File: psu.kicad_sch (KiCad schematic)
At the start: 30 parts, among them U1 TLS115, U3 LMR14020, U4 TJA1051T-3, U5 TJA1051T-3, U6 AMS1117-3.3

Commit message: update
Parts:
- added D19: SM15T33CA, Diode_SMD:D_SMC, symbol Device:D_TVS
- added D20: D_Schottky, Diode_SMD:D_SMA, symbol Device:D_Schottky
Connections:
- net 12v_PROT: now also D20.1 (K)
- net GND: now also D19.2 (A2)
- new net 12V_MR: D19.1 (A1), D20.2 (A)
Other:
- moved on the sheet: C2, C3, R1, U1

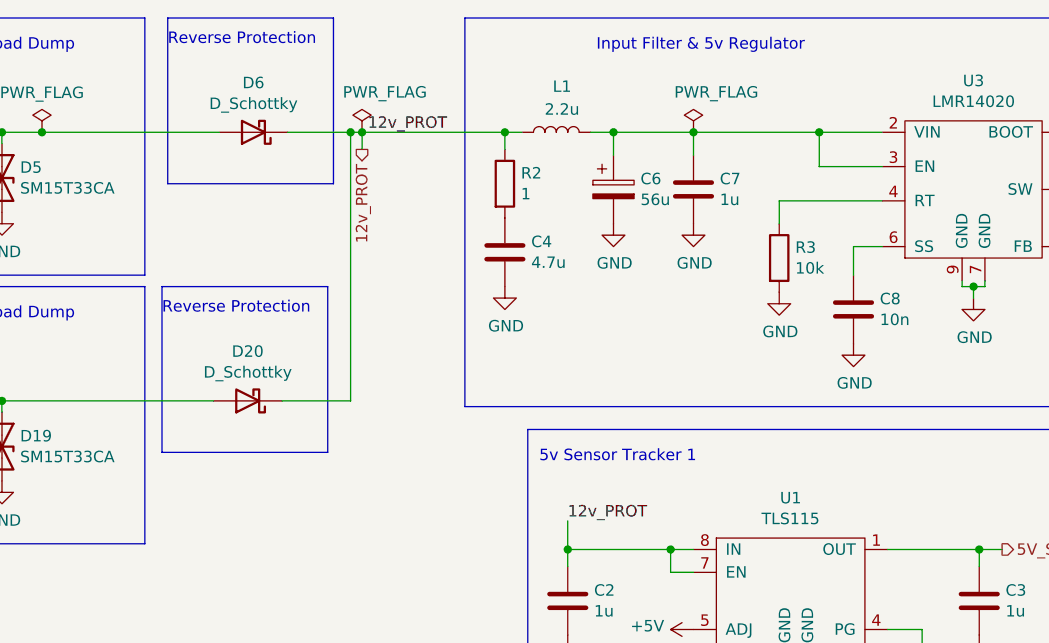
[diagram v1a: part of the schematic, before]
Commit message: Updates - Route digital inputs to connector - Add optional VR conditioner - Second Enable for H-Bridge
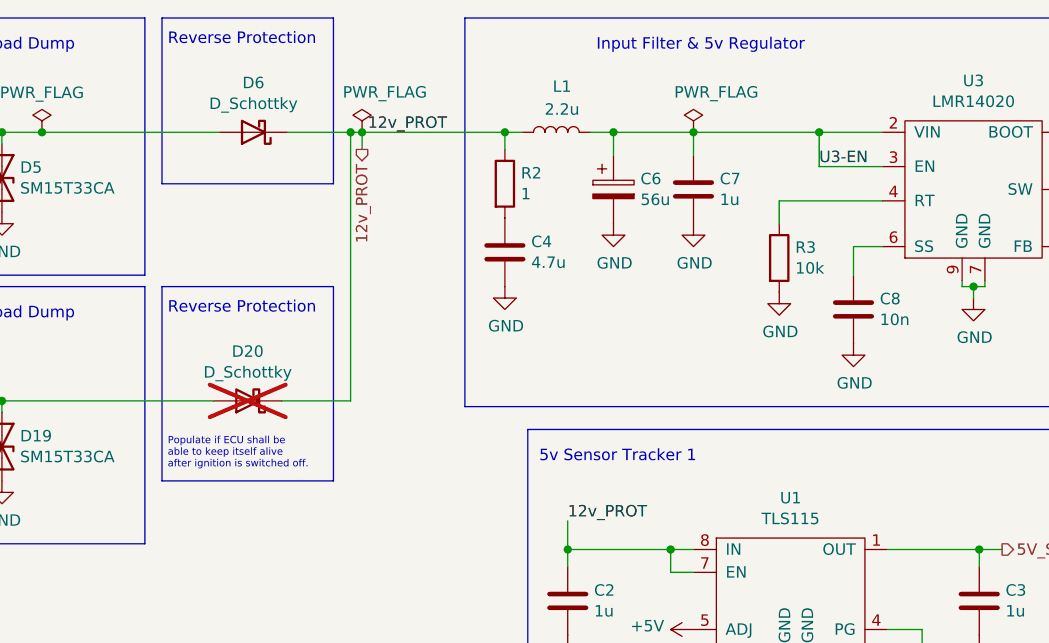
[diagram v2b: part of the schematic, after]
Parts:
- D20: now not fitted
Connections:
- net U3-EN: now reaches C6.1, C7.1, L1.2, U3.2 (VIN), U3.3 (EN)
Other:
- note added: "Populate if ECU shall be able to keep itself alive after ignition is switched off."
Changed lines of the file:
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@@
     (stroke (width 0) (type default))
   )
-  (polyline (pts (xy 50.165 16.51) (xy 68.58 16.51))
+  (polyline (pts (xy 49.53 16.51) (xy 68.58 16.51))
     (stroke (width 0) (type default))
   )
@@
     (stroke (width 0) (type default))
   )
-  (polyline (pts (xy 67.945 46.355) (xy 67.945 64.77))
+  (polyline (pts (xy 68.58 46.355) (xy 68.58 67.945))
     (stroke (width 0) (type default))
   )
@@
     (stroke (width 0) (type default))
   )
-  (polyline (pts (xy 49.53 46.355) (xy 67.945 46.355))
-    (stroke (width 0) (type default))
-  )
-  (polyline (pts (xy 68.58 34.925) (xy 50.165 34.925))
+  (polyline (pts (xy 49.53 46.355) (xy 68.58 46.355))
+    (stroke (width 0) (type default))
+  )
+  (polyline (pts (xy 68.58 34.925) (xy 49.53 34.925))
     (stroke (width 0) (type default))
   )
@@
     (stroke (width 0) (type default))
   )
-  (polyline (pts (xy 50.165 34.925) (xy 50.165 16.51))
+  (polyline (pts (xy 49.53 34.925) (xy 49.53 16.51))
     (stroke (width 0) (type default))
   )
@@
     (stroke (width 0) (type default))
   )
-  (polyline (pts (xy 67.945 64.77) (xy 49.53 64.77))
+  (polyline (pts (xy 68.58 67.945) (xy 49.53 67.945))
     (stroke (width 0) (type default))
   )
@@
     (stroke (width 0) (type default))
   )
-  (polyline (pts (xy 49.53 64.77) (xy 49.53 46.355))
+  (polyline (pts (xy 49.53 67.945) (xy 49.53 46.355))
     (stroke (width 0) (type default))
   )
@@
     (stroke (width 0) (type default))
   )
-  (text "Reverse Protection" (at 49.53 49.53 0)
+  (text "Populate if ECU shall be \nable to keep itself alive\nafter ignition is switched off."
+    (at 50.165 66.675 0)
+    (effects (font (size 0.8 0.8)) (justify left bottom))
+  )
+  (text "Reverse Protection" (at 50.165 49.53 0)
     (effects (font (size 1.27 1.27)) (justify left bottom))
   )
@@
   )
   (label "12v_PROT" (at 94.615 72.39 0) (fields_autoplaced)
+    (effects (font (size 1.27 1.27)) (justify left bottom))
+  )
+  (label "U3-EN" (at 122.555 33.02 0) (fields_autoplaced)
     (effects (font (size 1.27 1.27)) (justify left bottom))
   )
@@
   )
   (symbol (lib_id "Device:D_Schottky") (at 59.055 59.055 180) (unit 1)
-    (in_bom yes) (on_board yes) (dnp no)
+    (in_bom yes) (on_board yes) (dnp yes)
     (property "Reference" "D20" (at 59.055 53.5686 0)
       (effects (font (size 1.27 1.27)))

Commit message: USB jack, parts and LCSC numbers, headphone jack
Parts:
- C6: LCSC N/A -> C106564
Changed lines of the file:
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@@
       (effects (font (size 1.27 1.27)) hide)
     )
-    (property "LCSC" "N/A" (at 99.695 35.56 0)
+    (property "LCSC" "C106564" (at 99.695 35.56 0)
       (effects (font (size 1.27 1.27)) hide)
     )

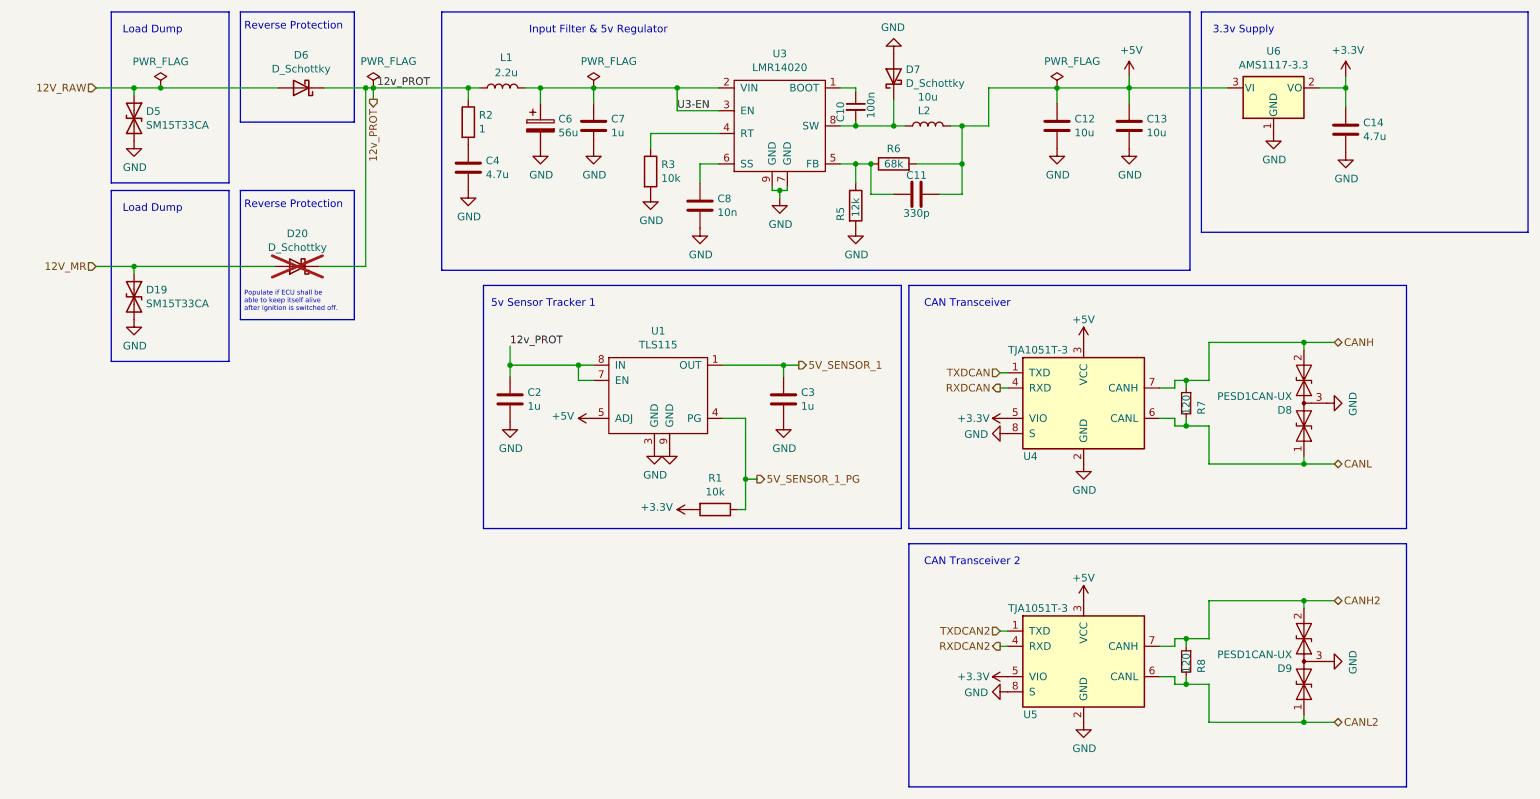
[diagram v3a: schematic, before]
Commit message: Add power LEDs, silkscreen beautifying, remove U11 use U10B
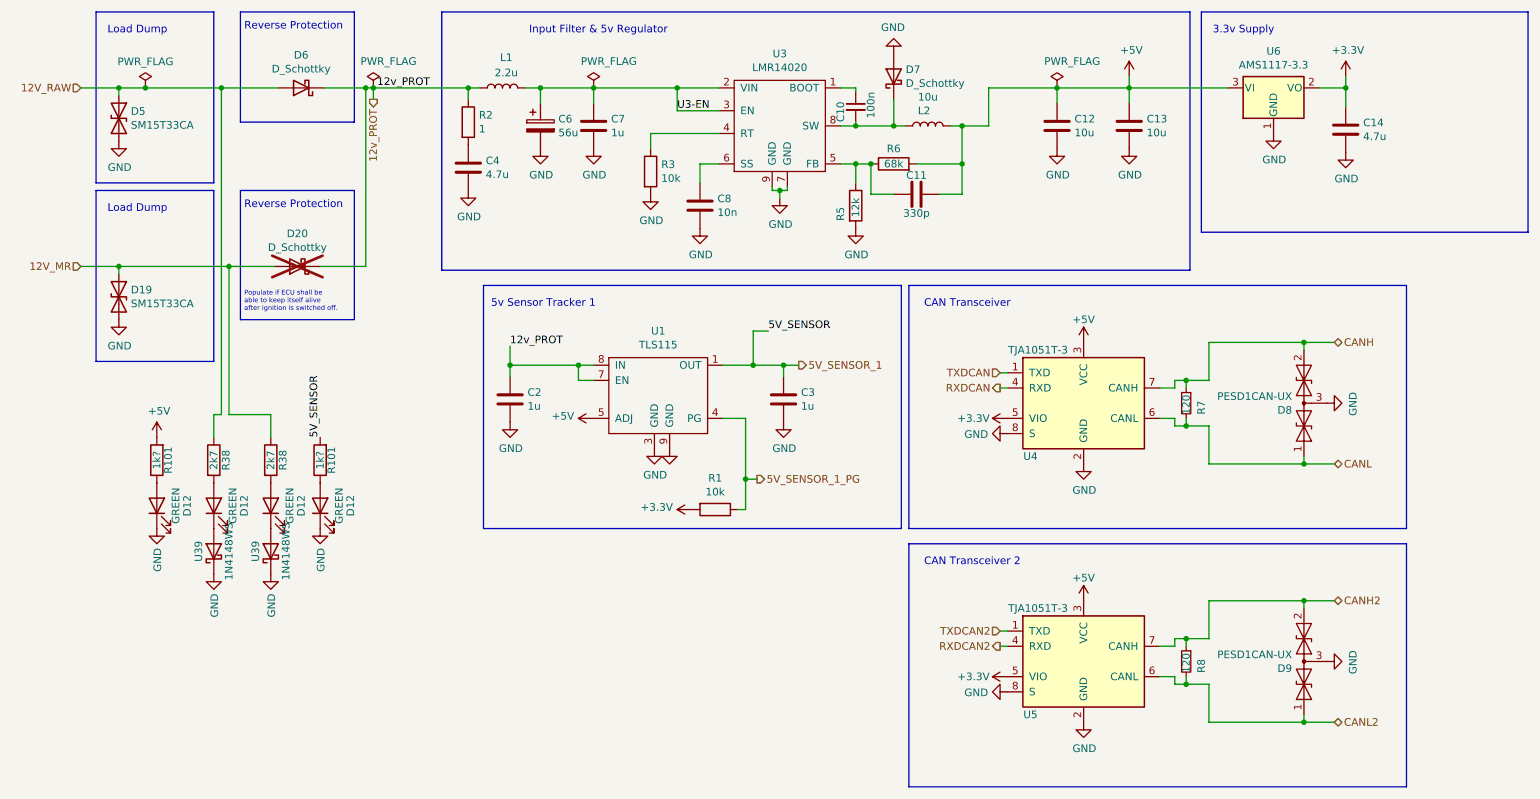
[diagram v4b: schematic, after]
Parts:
- added D12 (x4): GREEN, LED_SMD:LED_0603_1608Metric, symbol Device:LED
- added R101 (x2): 1k?, Resistor_SMD:R_0402_1005Metric, symbol Device:R
- added R38 (x2): 2k7, Resistor_SMD:R_0402_1005Metric, symbol Device:R
- added U39 (x2): 1N4148WS, Diode_SMD:D_SOD-323, symbol Device:D_Schottky
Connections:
- net +5V: now also R101.2
- net 12V_MR: now also R38.1
- net 12V_RAW: now also R38.1
- net 5V_SENSOR_1: now also R101.2
- net GND: now also D12.1 (K), D12.1 (K), U39.1 (K), U39.1 (K)
- new net: D12.1 (K), U39.2 (A) (x2)
- new net: D12.2 (A), R38.2 (x2)
- new net: D12.2 (A), R101.1 (x2)
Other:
- moved on the sheet: D19, D5

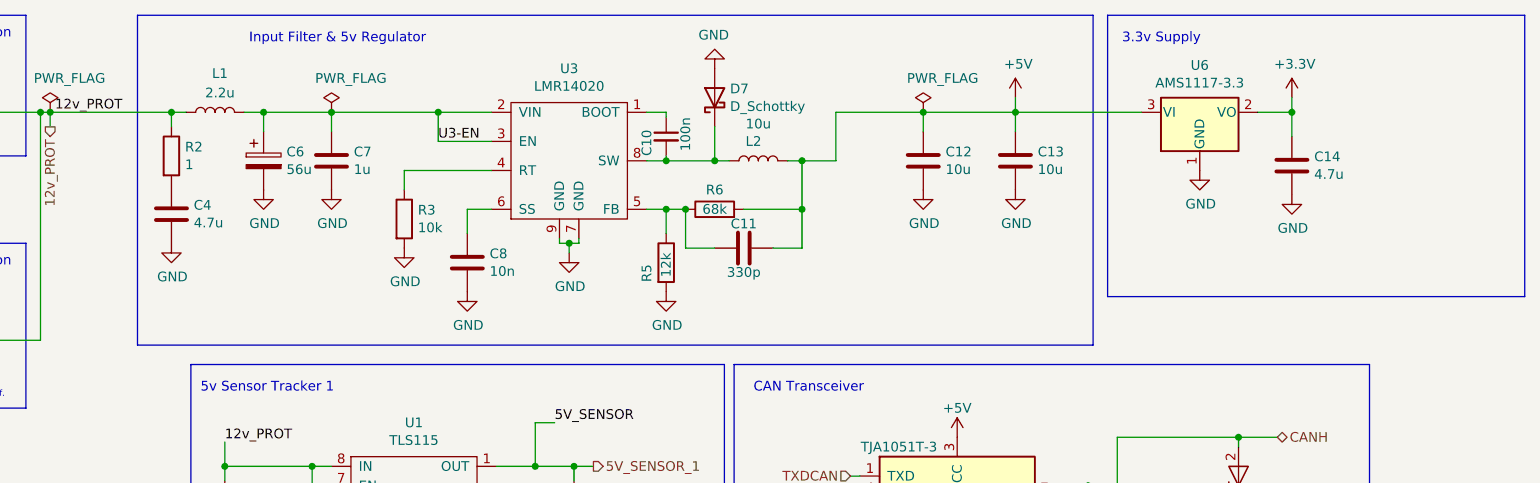
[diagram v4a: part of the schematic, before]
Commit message: Fix connector, optimize psu
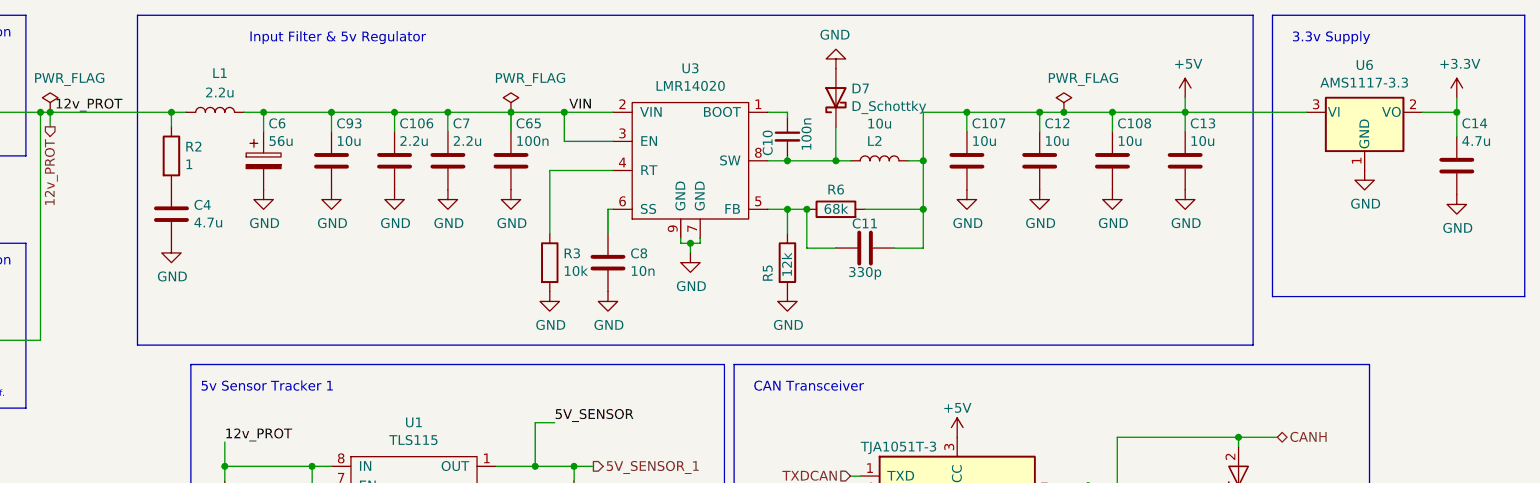
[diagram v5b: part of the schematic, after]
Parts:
- added C106: 2.2u, Capacitor_SMD:C_1206_3216Metric, symbol Device:C
- added C107, C108, C93: 10u, Capacitor_SMD:C_1206_3216Metric, symbol Device:C
- added C65: 100n, Capacitor_SMD:C_0603_1608Metric, symbol Device:C
- C4: footprint Capacitor_SMD:C_0603_1608Metric -> Capacitor_SMD:C_0805_2012Metric; LCSC C19666 -> C98192
- C7: value 1u -> 2.2u; footprint Capacitor_SMD:C_0603_1608Metric -> Capacitor_SMD:C_1206_3216Metric; LCSC C15849 -> C170101
- D20, D6, D7: LCSC C8678 -> C15874
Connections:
- net +5V: now also C107.1, C108.1
- net GND: now also C106.2, C107.2, C108.2, C65.2, C93.2
- net U3-EN renamed VIN
- net VIN: now also C106.1, C65.1, C93.1
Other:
- moved on the sheet: C10, C11, C12, C13, C14, C7, C8, D7, L2, R3, R5, R6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

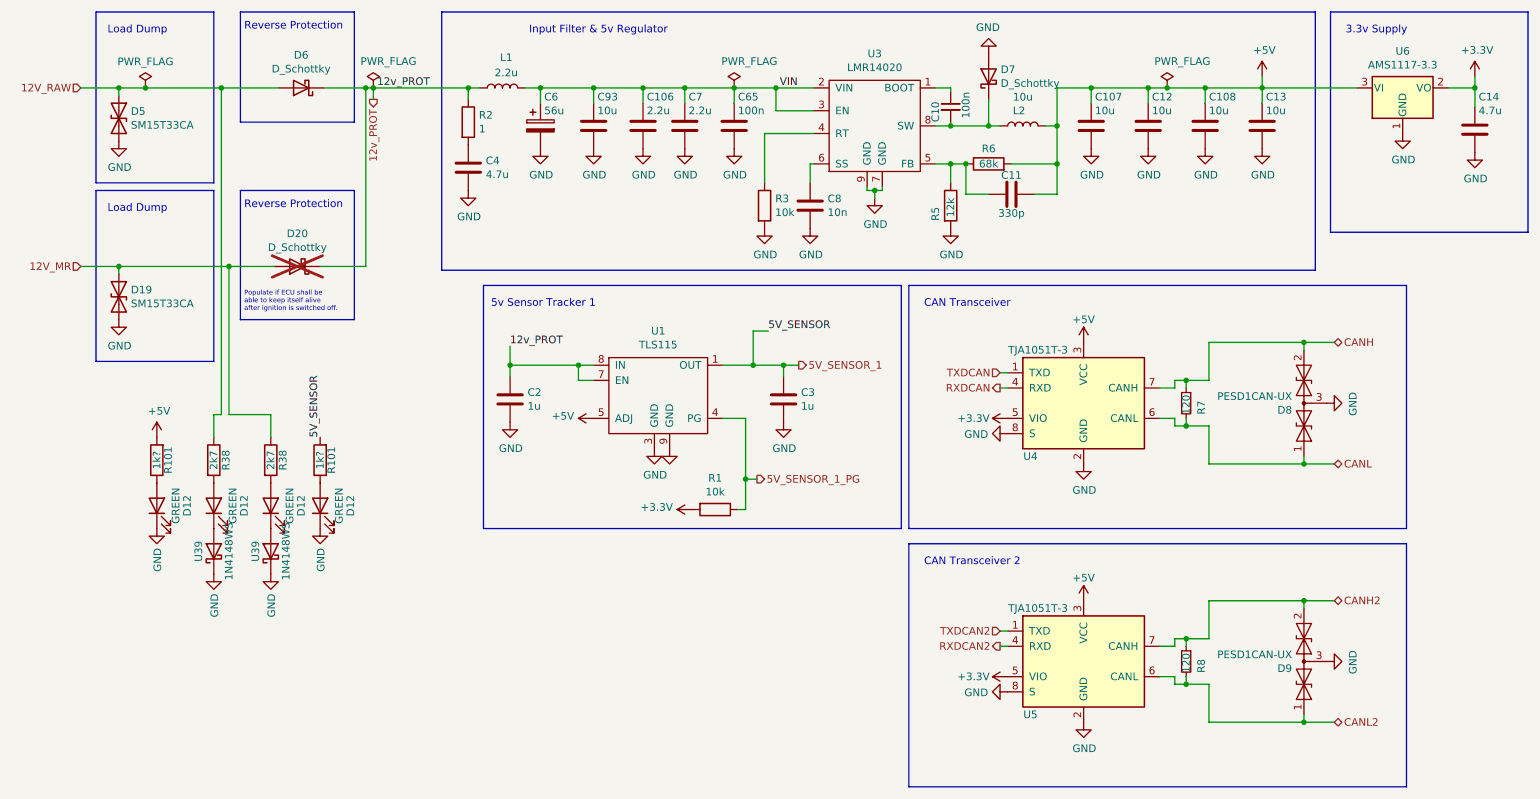
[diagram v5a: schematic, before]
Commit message: Add Stepper, fix Connector, add Testpoints, several changes
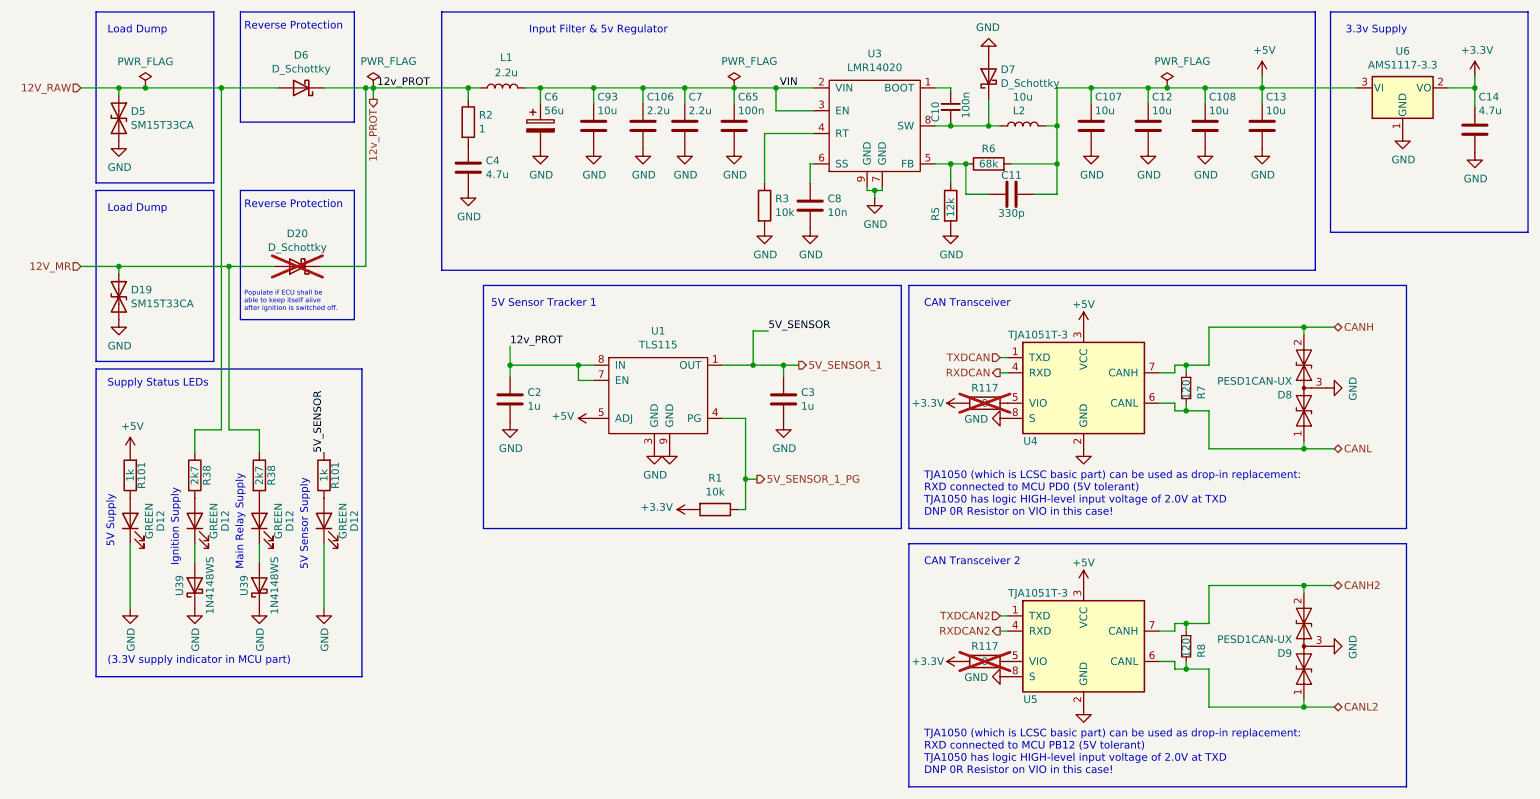
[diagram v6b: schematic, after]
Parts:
- added R117 (x2): 0, Resistor_SMD:R_0402_1005Metric, symbol Device:R
- D19, D5: LCSC_ext 1 -> C406701
- D20: LCSC C15874 -> C14996; now left out of the parts list
- D6, D7: LCSC C15874 -> C14996
- R101: value 1k? -> 1k; LCSC (none) -> C11702
- U39: LCSC C60580 -> C2128
- U4, U5: LCSC C38695 -> C6952
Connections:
- net +3V3: now also R117.1, R117.1; no longer U4.5 (VIO), U5.5 (VIO)
- new net: R117.2, U4.5 (VIO)
- new net: R117.2, U5.5 (VIO)
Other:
- note added: "(3.3V supply indicator in MCU part)"
- note added: "5V Sensor Supply"
- note added: "5V Sensor Tracker 1"
- note added: "5V Supply"
- note added: "Ignition Supply"
- note added: "Main Relay Supply"
- note added: "Supply Status LEDs"
- note added: "TJA1050 (which is LCSC basic part) can be used as drop-in replacement: RXD connected to MCU PB12 (5V tolerant) TJA1050 has logic HIGH-level input voltage of 2.0V at TXD DNP 0R Resistor on VIO in this case!"
- note added: "TJA1050 (which is LCSC basic part) can be used as drop-in replacement: RXD connected to MCU PD0 (5V tolerant) TJA1050 has logic HIGH-level input voltage of 2.0V at TXD DNP 0R Resistor on VIO in this case!"
- note removed: "5v Sensor Tracker 1"
- moved on the sheet: D12, D8, D9, R101, R38, R7, R8, U39, U4, U5
